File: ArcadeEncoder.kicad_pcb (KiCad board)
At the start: 2 copper layers, 59 x 46 mm, 8 parts, among them J1 DB15_Male, J2 DB9_Male, U1 ProMicro

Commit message: v0.2
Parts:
- moved REF** 58.7 mm to (117.0, 67.2)
- moved REF** 35.7 mm to (152.4, 46.9)
- moved REF** 3.39 mm to (167.6, 79.6)
- moved REF** 2.34 mm to (159.8, 79.5)
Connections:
- J2 pad 4: Net-(J2-Pad4) -> RIGHT
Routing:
- net RIGHT: track 29.3 -> 55.7 mm, vias 0 -> 2
- net B6: track 57.4 -> 56.7 mm
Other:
- board size 59 x 46 mm -> 56.6 x 38.7 mm
- board text added: "TOP"
- board text added: "https://github.com/klein0r/pcb-arcade-encoder"
- board text added: "v0.2"
- board text removed: "DaemonBite-Arcade-Encoder v0.1"

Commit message: Changes for sega
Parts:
- removed J1: DB15_Male, halibs:D-Sub_Connector_15P-Male
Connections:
- net DOWN renamed P2
- net LEFT renamed P3
- net RIGHT renamed P4
- net UP renamed P1
- J2 pad 5: B3 -> +5V
- J2 pad 6: B1 -> P6
- J2 pad 7: +5V -> P7
- J2 pad 9: B2 -> P9
- U1 pad 1: B4 -> Net-(U1-Pad1)
- U1 pad 10: Net-(U1-Pad10) -> P7
- U1 pad 14: B7 -> Net-(U1-Pad14)
- U1 pad 15: B8 -> P6
- U1 pad 16: B6 -> P9
- U1 pad 2: B3 -> Net-(U1-Pad2)
- U1 pad 5: B2 -> Net-(U1-Pad5)
- U1 pad 6: B1 -> Net-(U1-Pad6)
- U1 pad 7: B5 -> Net-(U1-Pad7)
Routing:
- net B8: track 66.3 -> 0.00 mm
- net B2: track 57.1 -> 0.00 mm
- net B6: track 56.7 -> 0.00 mm
- net B3: track 56.2 -> 0.00 mm
- net B1: track 45.0 -> 0.00 mm
- net B7: track 29.8 -> 0.00 mm
- net P6: track 0.00 -> 29.5 mm, vias 0 -> 1
- net P9: track 0.00 -> 27.9 mm, vias 0 -> 1
- net P7: track 0.00 -> 23.5 mm
- net P3: track 57.7 -> 34.7 mm, vias 0 -> 1
- net +5V: track 58.6 -> 37.2 mm, vias 1 -> 0
- net P2: track 53.7 -> 33.0 mm, vias 1 -> 0
- net P4: track 55.7 -> 35.9 mm, vias 2 -> 1
- net B4: track 19.7 -> 0.00 mm
- net P1: track 50.9 -> 31.6 mm, vias 0 -> 1
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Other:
- board text added: "(Sega Mega Drive)"
- board text added: "Solder J1 !!!"
- board text added: "v0.1 Sega"
- board text removed: "(Arcade Controller)"
- board text removed: "(Atari/C64/Amiga)"
- board text removed: "v0.2"

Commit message: Updated to KiCad 6
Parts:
- J2: footprint halibs:D-Sub_Connector_9P-Male -> haus-automatisierung:D-Sub_Connector_9P-Male
- U1: footprint halibs:ArduinoProMicro -> haus-automatisierung:ArduinoProMicro
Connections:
- U1 pad 1: Net-(U1-Pad1) -> unconnected-(U1-Pad1)
- U1 pad 11: Net-(U1-Pad11) -> unconnected-(U1-Pad11)
- U1 pad 12: Net-(U1-Pad12) -> unconnected-(U1-Pad12)
- U1 pad 13: Net-(U1-Pad13) -> unconnected-(U1-Pad13)
- U1 pad 14: Net-(U1-Pad14) -> unconnected-(U1-Pad14)
- U1 pad 2: Net-(U1-Pad2) -> unconnected-(U1-Pad2)
- U1 pad 22: Net-(U1-Pad22) -> unconnected-(U1-Pad22)
- U1 pad 24: Net-(U1-Pad24) -> unconnected-(U1-Pad24)
- U1 pad 5: Net-(U1-Pad5) -> unconnected-(U1-Pad5)
- U1 pad 6: Net-(U1-Pad6) -> unconnected-(U1-Pad6)
- U1 pad 7: Net-(U1-Pad7) -> unconnected-(U1-Pad7)
- U1 pad 8: Net-(U1-Pad8) -> unconnected-(U1-Pad8)
- U1 pad 9: Net-(U1-Pad9) -> unconnected-(U1-Pad9)
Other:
- net class Default removed

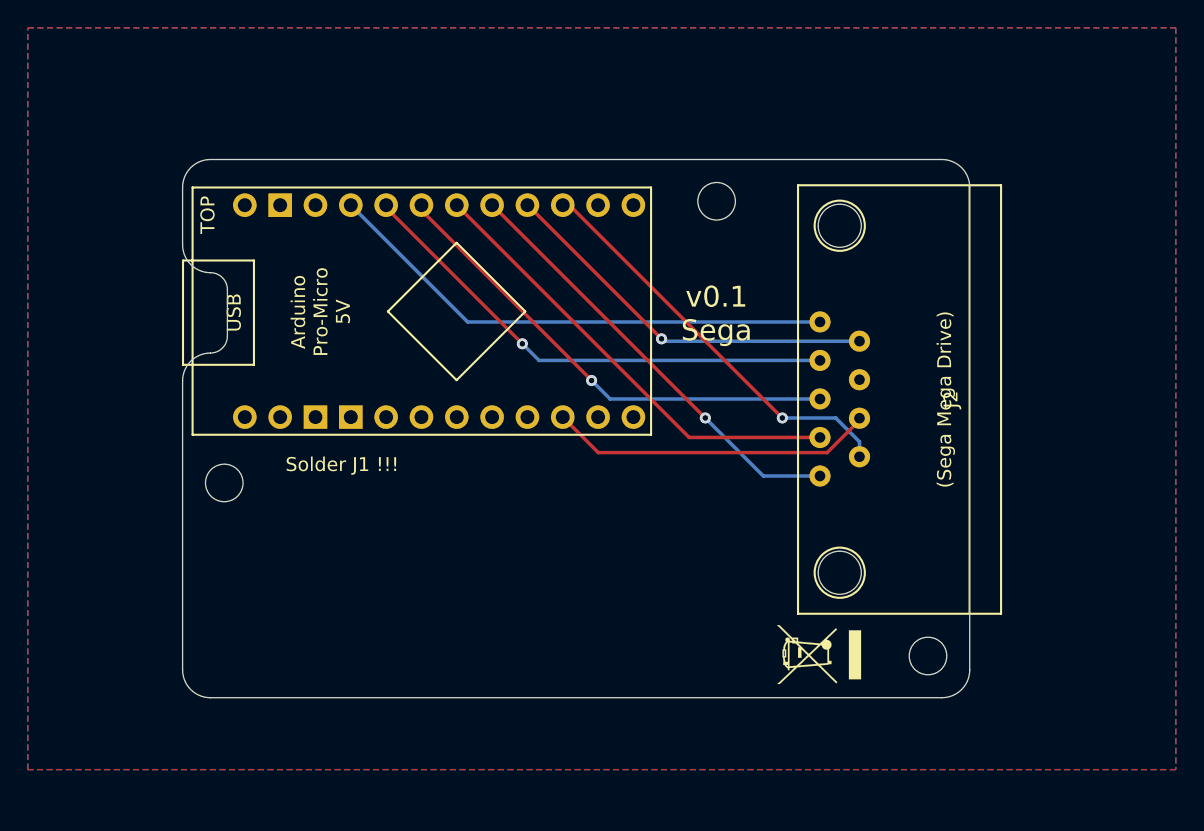
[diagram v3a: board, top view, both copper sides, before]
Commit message: Sony PSX Connector
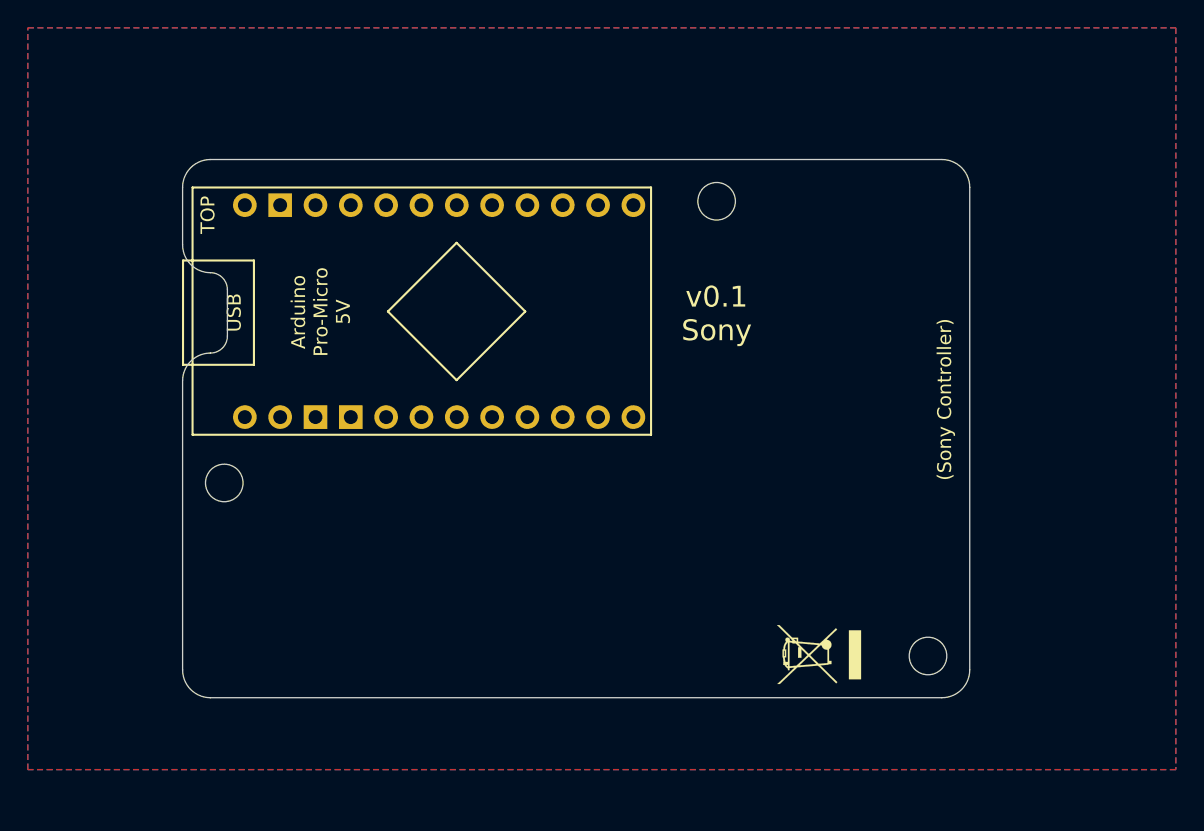
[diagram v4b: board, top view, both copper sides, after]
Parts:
- removed J2: DB9_Male, haus-automatisierung:D-Sub_Connector_9P-Male
- U1: value ProMicro -> ArduinoProMicro
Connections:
- U1 pad 10: P7 -> unconnected-(U1-Pad10)
- U1 pad 15: P6 -> unconnected-(U1-Pad15)
- U1 pad 16: P9 -> unconnected-(U1-Pad16)
- U1 pad 17: P1 -> DATA
- U1 pad 18: P2 -> unconnected-(U1-Pad18)
- U1 pad 19: P3 -> unconnected-(U1-Pad19)
- U1 pad 20: P4 -> unconnected-(U1-Pad20)
- U1 pad 5: unconnected-(U1-Pad5) -> CMD
- U1 pad 6: unconnected-(U1-Pad6) -> ATT
- U1 pad 7: unconnected-(U1-Pad7) -> CLK
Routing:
- net +5V: track 37.2 -> 0.00 mm
- net P4: track 35.9 -> 0.00 mm, vias 1 -> 0
- net P3: track 34.7 -> 0.00 mm, vias 1 -> 0
- net P2: track 33.0 -> 0.00 mm
- net P1: track 31.6 -> 0.00 mm, vias 1 -> 0
- net P6: track 29.5 -> 0.00 mm, vias 1 -> 0
- net P9: track 27.9 -> 0.00 mm, vias 1 -> 0
- net P7: track 23.5 -> 0.00 mm
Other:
- board text added: "(Sony Controller)"
- board text added: "v0.1 Sony"
- board text removed: "(Sega Mega Drive)"
- board text removed: "Solder J1 !!!"
- board text removed: "v0.1 Sega"
